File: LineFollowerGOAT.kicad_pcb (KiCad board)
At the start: 2 copper layers, 164 x 103.2 mm, 195 parts, among them J1 USB_C_Receptacle_USB2.0_14P, J10 Conn_01x20_MountingPin, J11 Conn_01x02_Pin, J12 XT30UPB-M, J13 XT30UPB-M, J15 XT30UPB-M, J16 HC-05 Breakout Board, J17 HC-05 Breakout Board, J18 Conn_01x02_Socket, J19 Conn_01x02_Socket, J2 Conn_01x04_Pin, J3 Conn_01x02_Pin, J4 Conn_01x02_Pin, J5 XT30UPB-M, J6 Conn_01x02_Pin, J7 Conn_01x20_MountingPin, J8 Conn_01x02_Pin, J9 Conn_01x20_MountingPin, SW1 SW_SPDT, SW10 SW_Push, SW12 SW_SPDT, SW13 SW_SPDT, SW2 SW_Push, SW3 SW_Push, SW5 Reset, SW6 SW_SPDT, SW8 SW_SPDT, SW9 SW_Push, U1 AMS1117-5.0, U10 TCRT5000L, U11 TCRT5000L, U12 STM32F103C8Tx, U13 AMS1117-3.3, U14 AMS1117-5.0, U15 AP62300TWU, U16 TCRT5000L, U17 TCRT5000L, U18 TCRT5000L, U2 AP62300TWU, U20 TCRT5000L, U21 TCRT5000L, U22 TCRT5000L, U23 74HC4067, U24 74HC4067, U27 TCRT5000L, U3 TCRT5000L, U4 TCRT5000L, U5 TCRT5000L, U6 TCRT5000L, U7 TCRT5000L, U8 TCRT5000L, U9 TCRT5000L, Y1 Crystal

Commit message: updated
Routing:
- net +3.3V: track 629.8 -> 620.9 mm
- net BAT+I: track 86.9 -> 83.7 mm
- net +5V: track 85.9 -> 88.4 mm
- net ESC_POWI: track 20.0 -> 20.5 mm, vias 3 -> 6
- net GND: vias 200 -> 205

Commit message: Corrected errors in PCB
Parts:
- moved J13 5.12 mm to (107.0, 105.0), turned to 0 degrees
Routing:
- net GND: track 346.0 -> 364.7 mm, vias 205 -> 266
- net +3.3V: track 620.9 -> 638.0 mm, vias 8 -> 10
- net Net-(R50-Pad2): track 1.91 -> 8.12 mm
- net ESC_POWI: track 20.5 -> 26.3 mm, vias 6 -> 7
- net Net-(J13-P): track 8.82 -> 6.23 mm
- net +5V: vias 4 -> 3

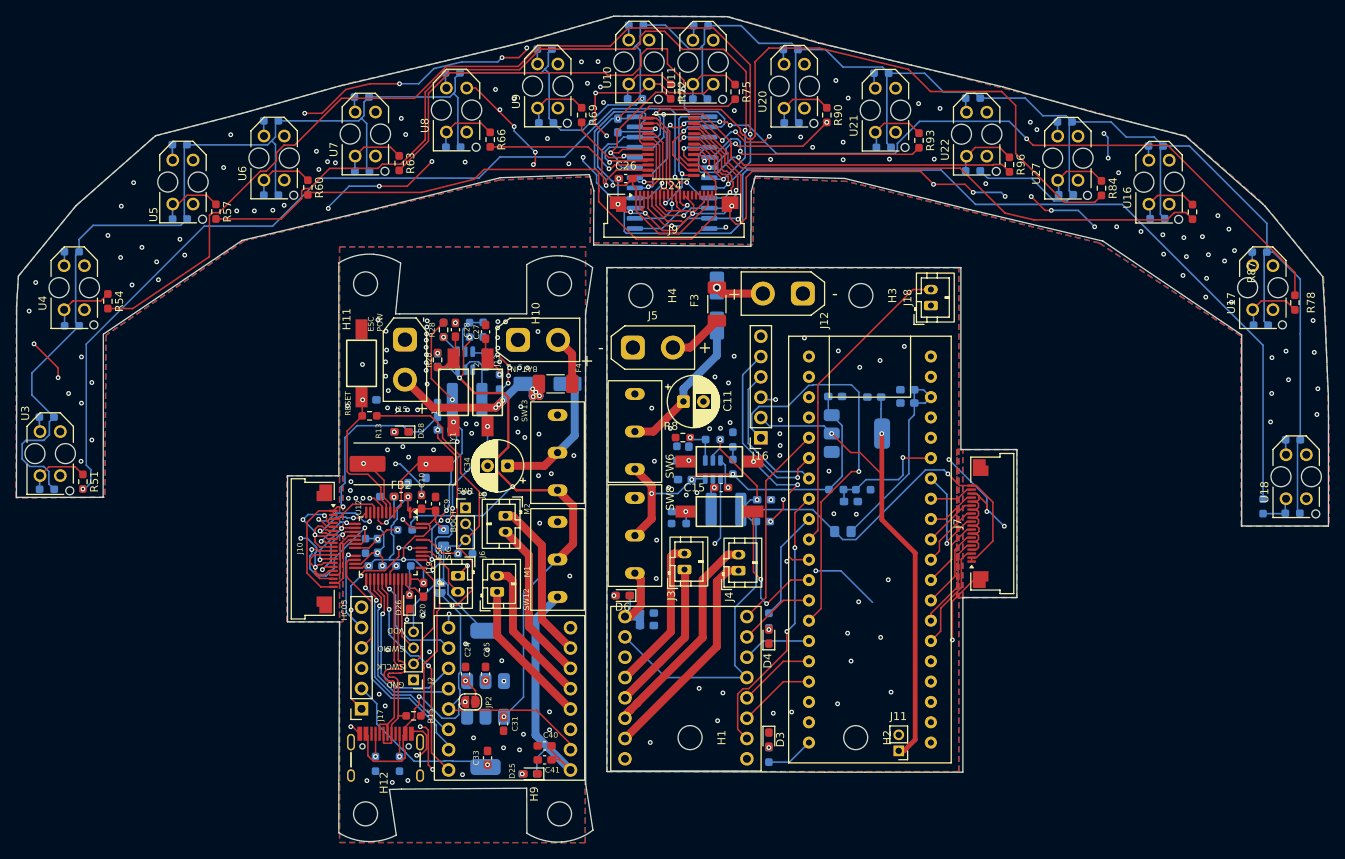
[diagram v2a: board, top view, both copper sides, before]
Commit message: Ground stiching done
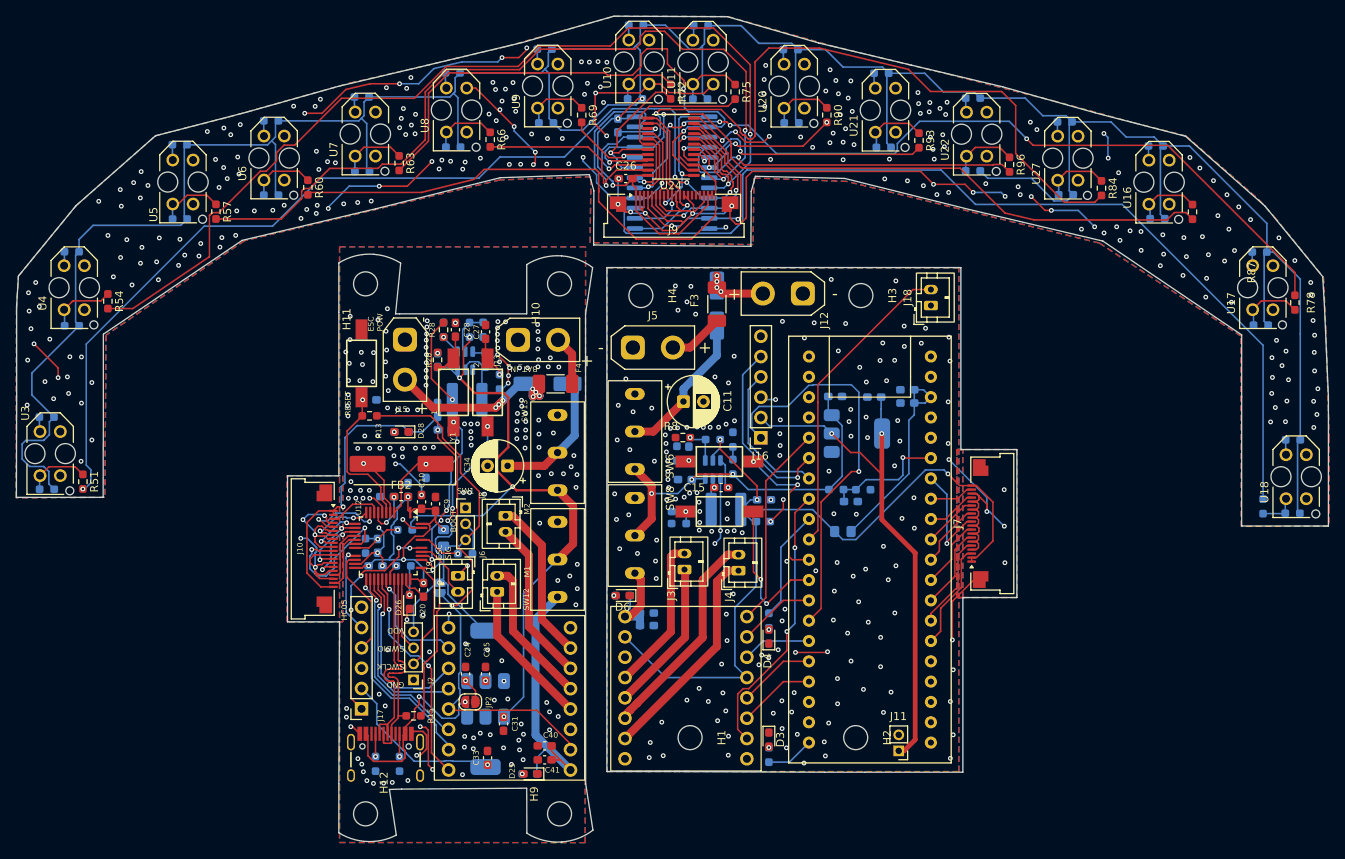
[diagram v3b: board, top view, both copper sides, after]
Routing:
- net GND: track 364.7 -> 360.0 mm, vias 266 -> 585
- net ESC_POW: track 6.06 -> 7.57 mm, vias 1 -> 4

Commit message: Updated
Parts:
- C15: value 10u -> 0.1u
- C29, C3: value 0.01u -> 47u
- R12, R27: value 10k -> 6.8k
- R26, R9: value 4.3k -> 51k
- R29, R8: value 1k -> 10k
- R3, R5, R7: value 1k -> 68
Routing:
- net GND: track 360.0 -> 363.1 mm, vias 585 -> 608

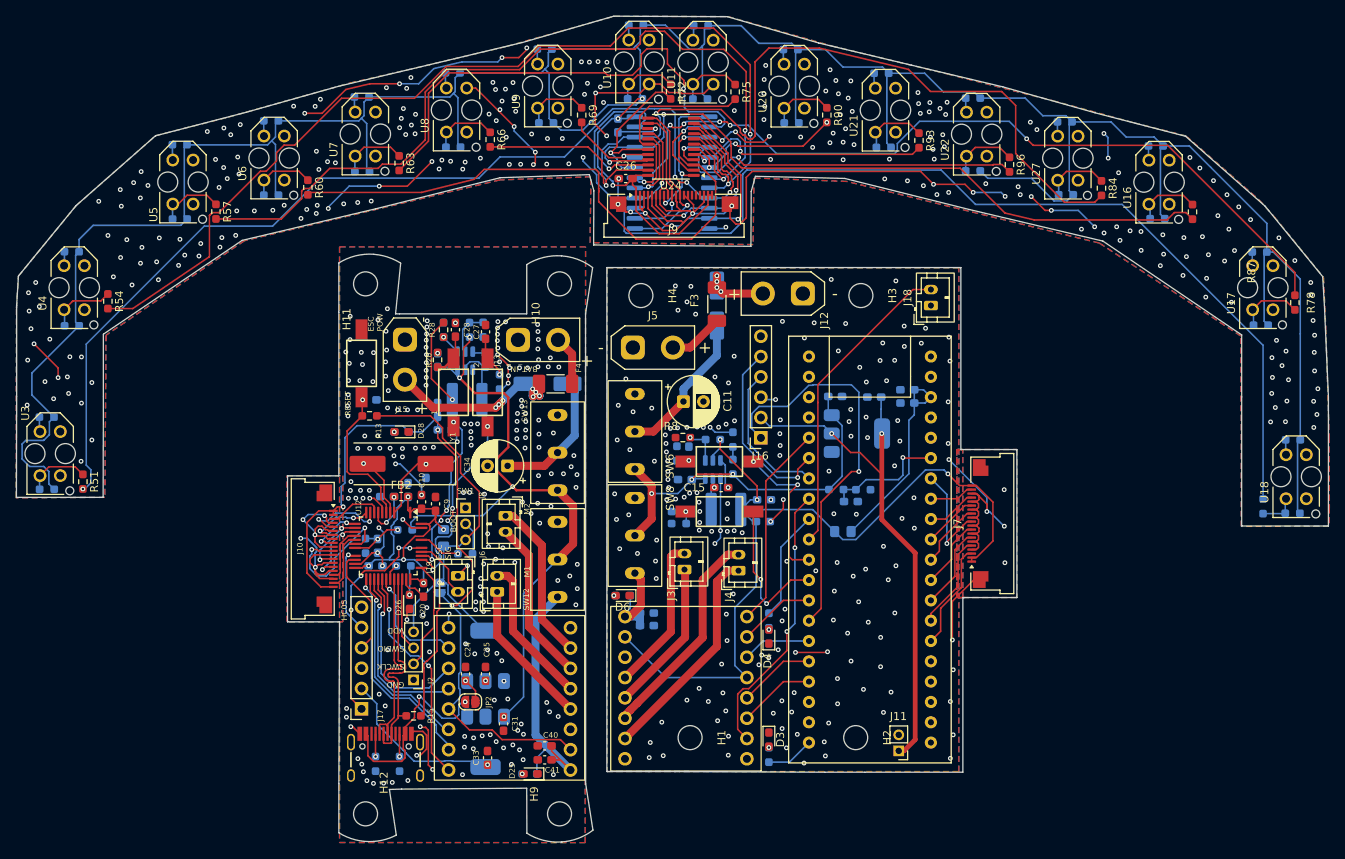
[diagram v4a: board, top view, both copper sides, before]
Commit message: Fixed Thermal Stokes Errors
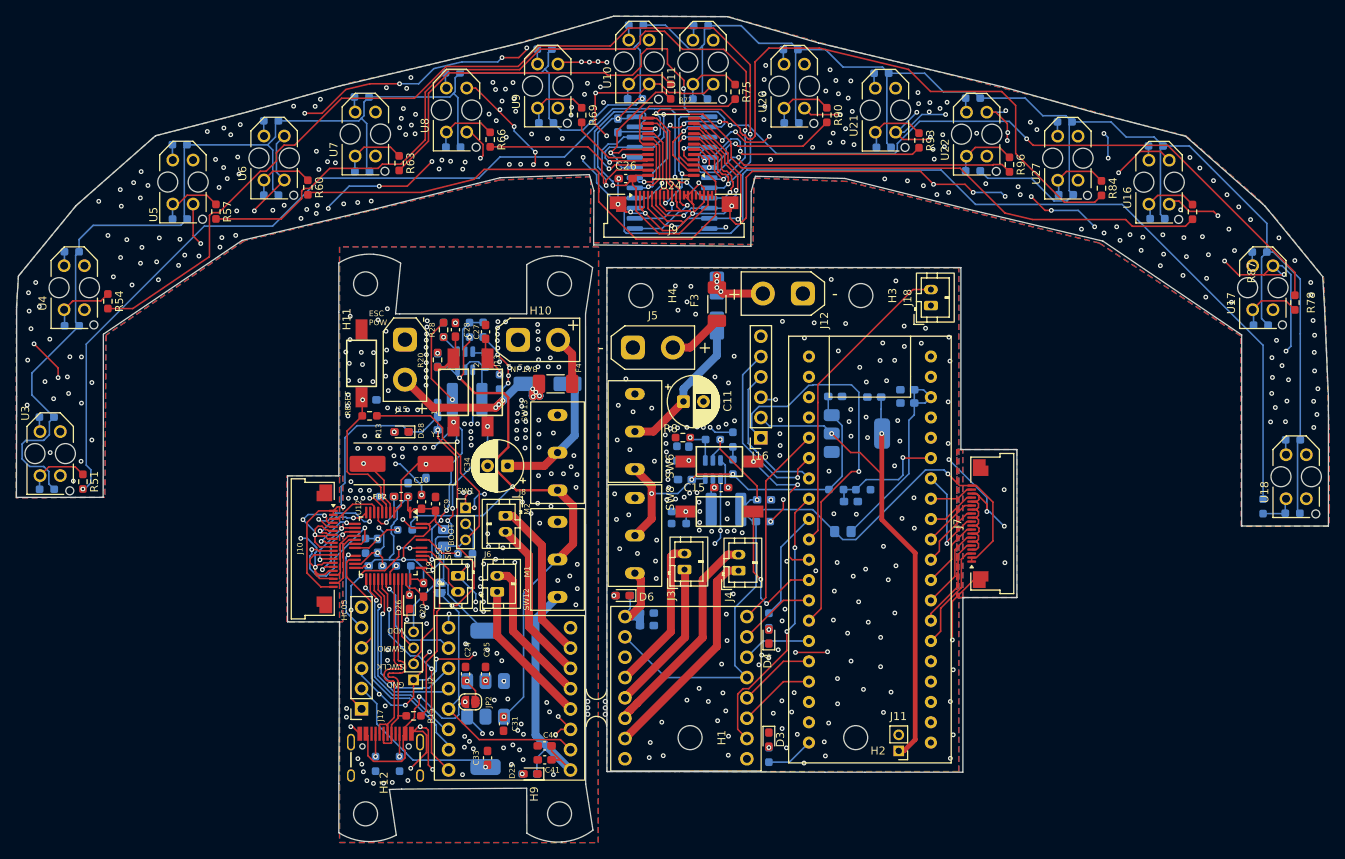
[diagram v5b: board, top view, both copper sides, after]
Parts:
- added mouse-bite-2.54mm-slot: VAL**, Mousebites:mouse-bite-2.54mm-slot, F.Cu at (116.8, 151.0)
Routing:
- net GND: track 363.1 -> 526.9 mm, vias 608 -> 621
- net Q4: vias 3 -> 2
